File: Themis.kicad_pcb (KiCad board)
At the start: 2 copper layers, 100 x 50 mm, 47 parts, among them J1 SMA, J10 Conn_01x01, J11 Conn_01x01, J12 Conn_01x01, J13 Conn_01x01, J14 SMA, J15 SMA, J16 SMA, J17 SMA, J18 Conn_01x01, J2 SMA, J20 Conn_01x01, J3 SMA, J4 SMA, J5 Conn_01x05, J6 SMA, J7 SMA, J8 SMA, J9 SMA, T1 Tr 1/33, T2 Tr 33/1, U1 LMC6482

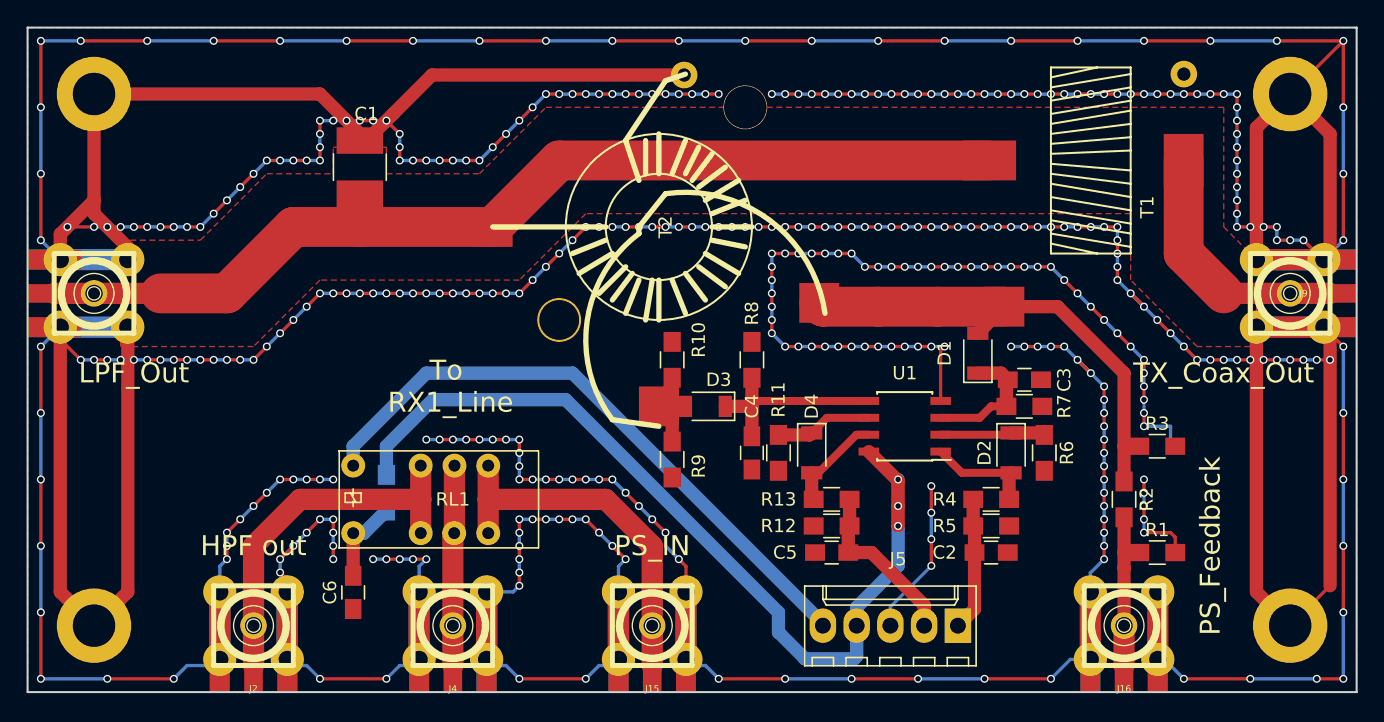
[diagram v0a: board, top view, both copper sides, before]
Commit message: BAT54 and transformer shielding added
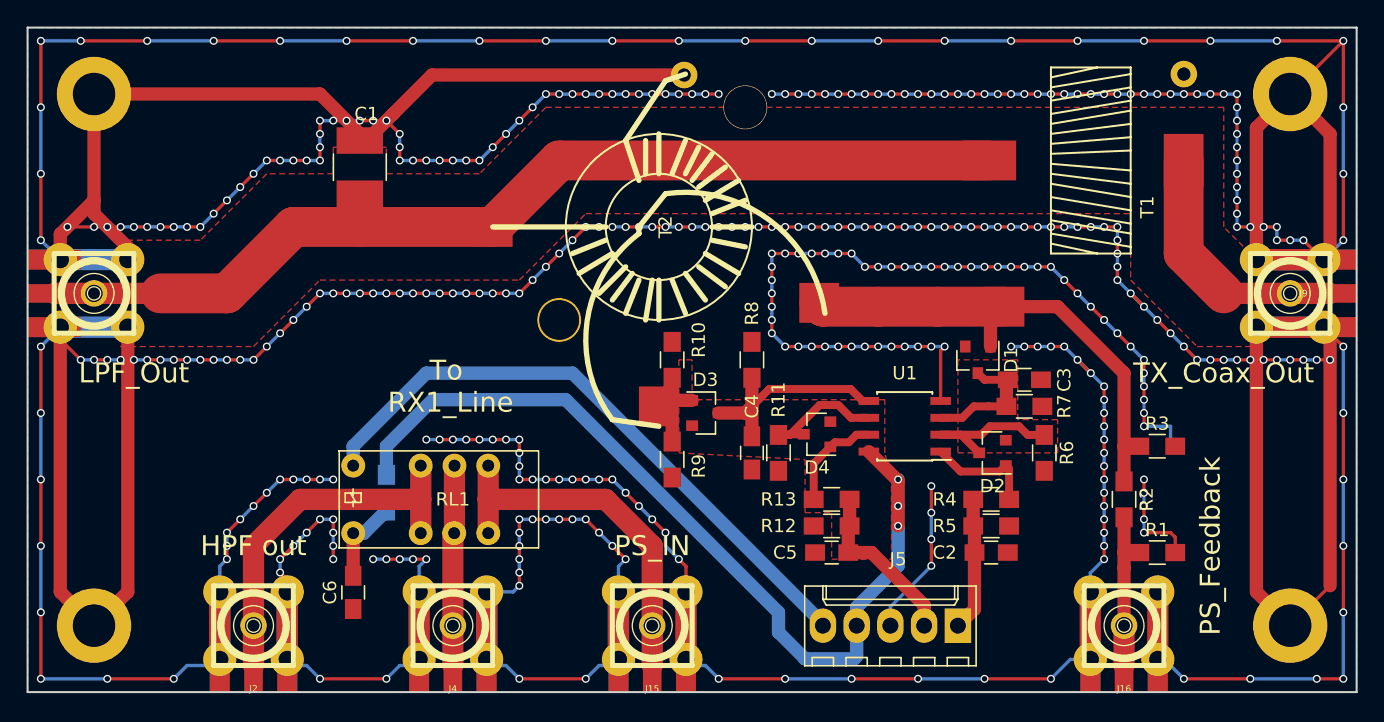
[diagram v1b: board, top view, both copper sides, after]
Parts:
- D1, D2, D3, D4: value D -> BAT54; footprint Diodes_SMD:D_1206 -> Diodes_SMD:D_SOT-23_ANK
- moved D4 1.46 mm to (149.4, 115.6), turned to 180 degrees
- moved D2 1.40 mm to (162.6, 117.0), turned to 180 degrees
- moved D1 0.50 mm to (161.5, 110.0), turned to 270 degrees
- moved D3 0.50 mm to (141.0, 114.0), turned to 0 degrees
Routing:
- net Net-(D2-Pad1): track 7.92 -> 11.8 mm
- net Net-(D4-Pad1): track 7.33 -> 10.1 mm
- net Net-(C4-Pad1): track 15.4 -> 16.8 mm
- net Net-(D3-Pad2): track 7.63 -> 8.31 mm
- net Net-(D1-Pad2): track 37.3 -> 37.9 mm

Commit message: via stitching added, new gerber
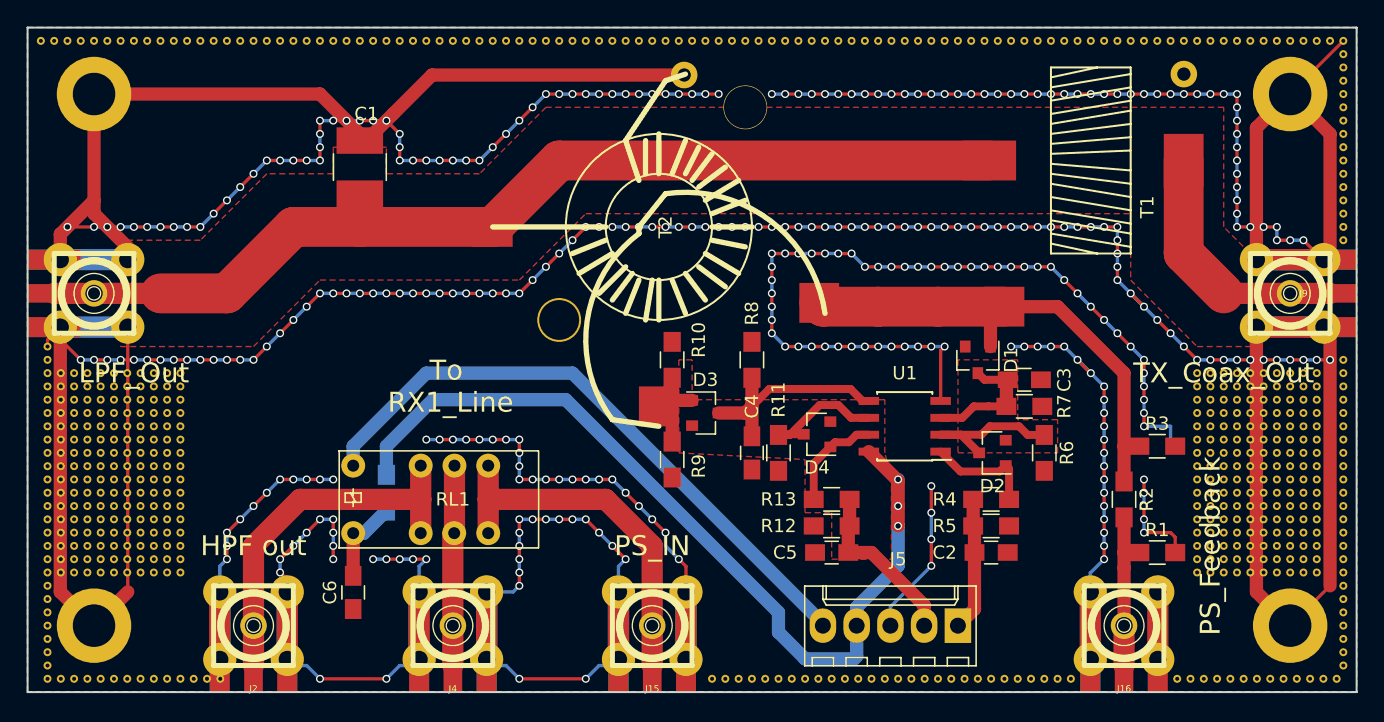
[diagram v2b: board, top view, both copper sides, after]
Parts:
- added REF**: via, via:via, F.Cu at (189.0, 101.0)
- added REF**: via, via:via, F.Cu at (189.0, 92.0)
- added REF**: via, via:via, F.Cu at (91.5, 128.0)
- added REF**: via, via:via, F.Cu at (91.5, 127.0)
- added REF**: via, via:via, F.Cu at (91.5, 126.0)
- added REF**: via, via:via, F.Cu at (91.5, 125.0)
- added REF**: via, via:via, F.Cu at (91.5, 124.0)
- added REF**: via, via:via, F.Cu at (91.5, 123.0)
- added REF**: via, via:via, F.Cu at (91.5, 122.0)
- added REF**: via, via:via, F.Cu at (91.5, 121.0)
- added REF**: via, via:via, F.Cu at (91.5, 120.0)
- added REF**: via, via:via, F.Cu at (91.5, 119.0)
- added REF**: via, via:via, F.Cu at (189.0, 91.0)
- added REF**: via, via:via, F.Cu at (91.5, 118.0)
- added REF**: via, via:via, F.Cu at (91.5, 117.0)
- added REF**: via, via:via, F.Cu at (91.5, 116.0)
- added REF**: via, via:via, F.Cu at (91.5, 115.0)
- added REF**: via, via:via, F.Cu at (91.5, 114.0)
- added REF**: via, via:via, F.Cu at (91.5, 113.0)
- added REF**: via, via:via, F.Cu at (91.5, 112.0)
- added REF**: via, via:via, F.Cu at (91.5, 111.0)
- added REF**: via, via:via, F.Cu at (91.5, 110.0)
- added REF**: via, via:via, F.Cu at (91.5, 109.0)
- added REF**: via, via:via, F.Cu at (189.0, 90.0)
- added REF**: via, via:via, F.Cu at (189.0, 86.0)
- added REF**: via, via:via, F.Cu at (188.0, 86.0)
- added REF**: via, via:via, F.Cu at (187.0, 86.0)
- added REF**: via, via:via, F.Cu at (186.0, 86.0)
- added REF**: via, via:via, F.Cu at (185.0, 86.0)
- added REF**: via, via:via, F.Cu at (184.0, 86.0)
- added REF**: via, via:via, F.Cu at (183.0, 86.0)
- added REF**: via, via:via, F.Cu at (182.0, 86.0)
- added REF**: via, via:via, F.Cu at (181.0, 86.0)
- added REF**: via, via:via, F.Cu at (180.0, 86.0)
- added REF**: via, via:via, F.Cu at (189.0, 89.0)
- added REF**: via, via:via, F.Cu at (179.0, 86.0)
- added REF**: via, via:via, F.Cu at (178.0, 86.0)
- added REF**: via, via:via, F.Cu at (177.0, 86.0)
- added REF**: via, via:via, F.Cu at (176.0, 86.0)
- added REF**: via, via:via, F.Cu at (175.0, 86.0)
- added REF**: via, via:via, F.Cu at (174.0, 86.0)
- added REF**: via, via:via, F.Cu at (173.0, 86.0)
- added REF**: via, via:via, F.Cu at (172.0, 86.0)
- added REF**: via, via:via, F.Cu at (171.0, 86.0)
- added REF**: via, via:via, F.Cu at (170.0, 86.0)
- added REF**: via, via:via, F.Cu at (189.0, 88.0)
- added REF**: via, via:via, F.Cu at (169.0, 86.0)
- added REF**: via, via:via, F.Cu at (168.0, 86.0)
- added REF**: via, via:via, F.Cu at (167.0, 86.0)
- added REF**: via, via:via, F.Cu at (166.0, 86.0)
- added REF**: via, via:via, F.Cu at (165.0, 86.0)
- added REF**: via, via:via, F.Cu at (164.0, 86.0)
- added REF**: via, via:via, F.Cu at (163.0, 86.0)
- added REF**: via, via:via, F.Cu at (162.0, 86.0)
- added REF**: via, via:via, F.Cu at (161.0, 86.0)
- added REF**: via, via:via, F.Cu at (160.0, 86.0)
- added REF**: via, via:via, F.Cu at (189.0, 87.0)
- added REF**: via, via:via, F.Cu at (159.0, 86.0)
- added REF**: via, via:via, F.Cu at (158.0, 86.0)
- added REF**: via, via:via, F.Cu at (157.0, 86.0)
- added REF**: via, via:via, F.Cu at (156.0, 86.0)
- added REF**: via, via:via, F.Cu at (155.0, 86.0)
- added REF**: via, via:via, F.Cu at (154.0, 86.0)
- added REF**: via, via:via, F.Cu at (153.0, 86.0)
- added REF**: via, via:via, F.Cu at (152.0, 86.0)
- added REF**: via, via:via, F.Cu at (151.0, 86.0)
- added REF**: via, via:via, F.Cu at (150.0, 86.0)
- added REF**: via, via:via, F.Cu at (189.0, 133.0)
- added REF**: via, via:via, F.Cu at (149.0, 86.0)
- added REF**: via, via:via, F.Cu at (148.0, 86.0)
- added REF**: via, via:via, F.Cu at (147.0, 86.0)
- added REF**: via, via:via, F.Cu at (146.0, 86.0)
- added REF**: via, via:via, F.Cu at (145.0, 86.0)
- added REF**: via, via:via, F.Cu at (144.0, 86.0)
- added REF**: via, via:via, F.Cu at (143.0, 86.0)
- added REF**: via, via:via, F.Cu at (142.0, 86.0)
- added REF**: via, via:via, F.Cu at (141.0, 86.0)
- added REF**: via, via:via, F.Cu at (140.0, 86.0)
- added REF**: via, via:via, F.Cu at (189.0, 132.0)
- added REF**: via, via:via, F.Cu at (139.0, 86.0)
- added REF**: via, via:via, F.Cu at (138.0, 86.0)
- added REF**: via, via:via, F.Cu at (137.0, 86.0)
- added REF**: via, via:via, F.Cu at (136.0, 86.0)
- added REF**: via, via:via, F.Cu at (135.0, 86.0)
- added REF**: via, via:via, F.Cu at (134.0, 86.0)
- added REF**: via, via:via, F.Cu at (133.0, 86.0)
- added REF**: via, via:via, F.Cu at (132.0, 86.0)
- added REF**: via, via:via, F.Cu at (131.0, 86.0)
- added REF**: via, via:via, F.Cu at (130.0, 86.0)
- added REF**: via, via:via, F.Cu at (189.0, 131.0)
- added REF**: via, via:via, F.Cu at (129.0, 86.0)
- added REF**: via, via:via, F.Cu at (128.0, 86.0)
- added REF**: via, via:via, F.Cu at (127.0, 86.0)
- added REF**: via, via:via, F.Cu at (126.0, 86.0)
- added REF**: via, via:via, F.Cu at (125.0, 86.0)
- added REF**: via, via:via, F.Cu at (124.0, 86.0)
- added REF**: via, via:via, F.Cu at (123.0, 86.0)
- added REF**: via, via:via, F.Cu at (122.0, 86.0)
- added REF**: via, via:via, F.Cu at (121.0, 86.0)
- added REF**: via, via:via, F.Cu at (120.0, 86.0)
- added REF**: via, via:via, F.Cu at (189.0, 130.0)
- added REF**: via, via:via, F.Cu at (119.0, 86.0)
- added REF**: via, via:via, F.Cu at (118.0, 86.0)
- added REF**: via, via:via, F.Cu at (117.0, 86.0)
- added REF**: via, via:via, F.Cu at (116.0, 86.0)
- added REF**: via, via:via, F.Cu at (115.0, 86.0)
- added REF**: via, via:via, F.Cu at (114.0, 86.0)
- added REF**: via, via:via, F.Cu at (113.0, 86.0)
- added REF**: via, via:via, F.Cu at (112.0, 86.0)
- added REF**: via, via:via, F.Cu at (111.0, 86.0)
- added REF**: via, via:via, F.Cu at (110.0, 86.0)
- added REF**: via, via:via, F.Cu at (189.0, 100.0)
- added REF**: via, via:via, F.Cu at (189.0, 129.0)
- added REF**: via, via:via, F.Cu at (109.0, 86.0)
- added REF**: via, via:via, F.Cu at (108.0, 86.0)
- added REF**: via, via:via, F.Cu at (107.0, 86.0)
- added REF**: via, via:via, F.Cu at (106.0, 86.0)
- added REF**: via, via:via, F.Cu at (105.0, 86.0)
- added REF**: via, via:via, F.Cu at (104.0, 86.0)
- added REF**: via, via:via, F.Cu at (103.0, 86.0)
- added REF**: via, via:via, F.Cu at (102.0, 86.0)
- added REF**: via, via:via, F.Cu at (101.0, 86.0)
- added REF**: via, via:via, F.Cu at (100.0, 86.0)
- added REF**: via, via:via, F.Cu at (189.0, 128.0)
- added REF**: via, via:via, F.Cu at (99.0, 86.0)
- added REF**: via, via:via, F.Cu at (98.0, 86.0)
- added REF**: via, via:via, F.Cu at (97.0, 86.0)
- added REF**: via, via:via, F.Cu at (96.0, 86.0)
- added REF**: via, via:via, F.Cu at (95.0, 86.0)
- added REF**: via, via:via, F.Cu at (94.0, 86.0)
- added REF**: via, via:via, F.Cu at (93.0, 86.0)
- added REF**: via, via:via, F.Cu at (92.0, 86.0)
- added REF**: via, via:via, F.Cu at (101.5, 126.0)
- added REF**: via, via:via, F.Cu at (100.5, 126.0)
- added REF**: via, via:via, F.Cu at (189.0, 127.0)
- added REF**: via, via:via, F.Cu at (99.5, 126.0)
- added REF**: via, via:via, F.Cu at (98.5, 126.0)
- added REF**: via, via:via, F.Cu at (97.5, 126.0)
- added REF**: via, via:via, F.Cu at (96.5, 126.0)
- added REF**: via, via:via, F.Cu at (95.5, 126.0)
- added REF**: via, via:via, F.Cu at (94.5, 126.0)
- added REF**: via, via:via, F.Cu at (93.5, 126.0)
- added REF**: via, via:via, F.Cu at (92.5, 126.0)
- added REF**: via, via:via, F.Cu at (101.5, 125.0)
- added REF**: via, via:via, F.Cu at (100.5, 125.0)
- added REF**: via, via:via, F.Cu at (189.0, 126.0)
- added REF**: via, via:via, F.Cu at (99.5, 125.0)
- added REF**: via, via:via, F.Cu at (98.5, 125.0)
- added REF**: via, via:via, F.Cu at (97.5, 125.0)
- added REF**: via, via:via, F.Cu at (96.5, 125.0)
- added REF**: via, via:via, F.Cu at (95.5, 125.0)
- added REF**: via, via:via, F.Cu at (94.5, 125.0)
- added REF**: via, via:via, F.Cu at (93.5, 125.0)
- added REF**: via, via:via, F.Cu at (92.5, 125.0)
- added REF**: via, via:via, F.Cu at (101.5, 124.0)
- added REF**: via, via:via, F.Cu at (100.5, 124.0)
- added REF**: via, via:via, F.Cu at (189.0, 125.0)
- added REF**: via, via:via, F.Cu at (99.5, 124.0)
- added REF**: via, via:via, F.Cu at (98.5, 124.0)
- added REF**: via, via:via, F.Cu at (97.5, 124.0)
- added REF**: via, via:via, F.Cu at (96.5, 124.0)
- added REF**: via, via:via, F.Cu at (95.5, 124.0)
- added REF**: via, via:via, F.Cu at (94.5, 124.0)
- added REF**: via, via:via, F.Cu at (93.5, 124.0)
- added REF**: via, via:via, F.Cu at (92.5, 124.0)
- added REF**: via, via:via, F.Cu at (101.5, 123.0)
- added REF**: via, via:via, F.Cu at (100.5, 123.0)
- added REF**: via, via:via, F.Cu at (189.0, 124.0)
- added REF**: via, via:via, F.Cu at (99.5, 123.0)
- added REF**: via, via:via, F.Cu at (98.5, 123.0)
- added REF**: via, via:via, F.Cu at (97.5, 123.0)
- added REF**: via, via:via, F.Cu at (96.5, 123.0)
- added REF**: via, via:via, F.Cu at (95.5, 123.0)
- added REF**: via, via:via, F.Cu at (94.5, 123.0)
- added REF**: via, via:via, F.Cu at (93.5, 123.0)
- added REF**: via, via:via, F.Cu at (92.5, 123.0)
- added REF**: via, via:via, F.Cu at (101.5, 122.0)
- added REF**: via, via:via, F.Cu at (100.5, 122.0)
- added REF**: via, via:via, F.Cu at (189.0, 123.0)
- added REF**: via, via:via, F.Cu at (99.5, 122.0)
- added REF**: via, via:via, F.Cu at (98.5, 122.0)
- added REF**: via, via:via, F.Cu at (97.5, 122.0)
- added REF**: via, via:via, F.Cu at (96.5, 122.0)
- added REF**: via, via:via, F.Cu at (95.5, 122.0)
- added REF**: via, via:via, F.Cu at (94.5, 122.0)
- added REF**: via, via:via, F.Cu at (93.5, 122.0)
- added REF**: via, via:via, F.Cu at (92.5, 122.0)
- added REF**: via, via:via, F.Cu at (101.5, 121.0)
- added REF**: via, via:via, F.Cu at (100.5, 121.0)
- added REF**: via, via:via, F.Cu at (189.0, 122.0)
- added REF**: via, via:via, F.Cu at (99.5, 121.0)
- added REF**: via, via:via, F.Cu at (98.5, 121.0)
- added REF**: via, via:via, F.Cu at (97.5, 121.0)
- added REF**: via, via:via, F.Cu at (96.5, 121.0)
- added REF**: via, via:via, F.Cu at (95.5, 121.0)
- added REF**: via, via:via, F.Cu at (94.5, 121.0)
- added REF**: via, via:via, F.Cu at (93.5, 121.0)
- added REF**: via, via:via, F.Cu at (92.5, 121.0)
- added REF**: via, via:via, F.Cu at (101.5, 120.0)
- added REF**: via, via:via, F.Cu at (100.5, 120.0)
- added REF**: via, via:via, F.Cu at (189.0, 121.0)
- added REF**: via, via:via, F.Cu at (99.5, 120.0)
- added REF**: via, via:via, F.Cu at (98.5, 120.0)
- added REF**: via, via:via, F.Cu at (97.5, 120.0)
- added REF**: via, via:via, F.Cu at (96.5, 120.0)
- added REF**: via, via:via, F.Cu at (95.5, 120.0)
- added REF**: via, via:via, F.Cu at (94.5, 120.0)
- added REF**: via, via:via, F.Cu at (93.5, 120.0)
- added REF**: via, via:via, F.Cu at (92.5, 120.0)
- added REF**: via, via:via, F.Cu at (101.5, 119.0)
- added REF**: via, via:via, F.Cu at (100.5, 119.0)
- added REF**: via, via:via, F.Cu at (189.0, 120.0)
- added REF**: via, via:via, F.Cu at (99.5, 119.0)
- added REF**: via, via:via, F.Cu at (98.5, 119.0)
- added REF**: via, via:via, F.Cu at (97.5, 119.0)
- added REF**: via, via:via, F.Cu at (96.5, 119.0)
- added REF**: via, via:via, F.Cu at (95.5, 119.0)
- added REF**: via, via:via, F.Cu at (94.5, 119.0)
- added REF**: via, via:via, F.Cu at (93.5, 119.0)
- added REF**: via, via:via, F.Cu at (92.5, 119.0)
- added REF**: via, via:via, F.Cu at (101.5, 118.0)
- added REF**: via, via:via, F.Cu at (100.5, 118.0)
- added REF**: via, via:via, F.Cu at (189.0, 99.0)
- added REF**: via, via:via, F.Cu at (189.0, 119.0)
- added REF**: via, via:via, F.Cu at (99.5, 118.0)
- added REF**: via, via:via, F.Cu at (98.5, 118.0)
- added REF**: via, via:via, F.Cu at (97.5, 118.0)
- added REF**: via, via:via, F.Cu at (96.5, 118.0)
- added REF**: via, via:via, F.Cu at (95.5, 118.0)
- added REF**: via, via:via, F.Cu at (94.5, 118.0)
- added REF**: via, via:via, F.Cu at (93.5, 118.0)
- added REF**: via, via:via, F.Cu at (92.5, 118.0)
- added REF**: via, via:via, F.Cu at (101.5, 117.0)
- added REF**: via, via:via, F.Cu at (100.5, 117.0)
- added REF**: via, via:via, F.Cu at (189.0, 118.0)
- added REF**: via, via:via, F.Cu at (99.5, 117.0)
- added REF**: via, via:via, F.Cu at (98.5, 117.0)
- added REF**: via, via:via, F.Cu at (97.5, 117.0)
- added REF**: via, via:via, F.Cu at (96.5, 117.0)
- added REF**: via, via:via, F.Cu at (95.5, 117.0)
- added REF**: via, via:via, F.Cu at (94.5, 117.0)
- added REF**: via, via:via, F.Cu at (93.5, 117.0)
- added REF**: via, via:via, F.Cu at (92.5, 117.0)
- added REF**: via, via:via, F.Cu at (101.5, 116.0)
- added REF**: via, via:via, F.Cu at (100.5, 116.0)
- added REF**: via, via:via, F.Cu at (189.0, 117.0)
- added REF**: via, via:via, F.Cu at (99.5, 116.0)
- added REF**: via, via:via, F.Cu at (98.5, 116.0)
- added REF**: via, via:via, F.Cu at (97.5, 116.0)
- added REF**: via, via:via, F.Cu at (96.5, 116.0)
- added REF**: via, via:via, F.Cu at (95.5, 116.0)
- added REF**: via, via:via, F.Cu at (94.5, 116.0)
- added REF**: via, via:via, F.Cu at (93.5, 116.0)
- added REF**: via, via:via, F.Cu at (92.5, 116.0)
- added REF**: via, via:via, F.Cu at (101.5, 115.0)
- added REF**: via, via:via, F.Cu at (100.5, 115.0)
- added REF**: via, via:via, F.Cu at (189.0, 116.0)
- added REF**: via, via:via, F.Cu at (99.5, 115.0)
- added REF**: via, via:via, F.Cu at (98.5, 115.0)
- added REF**: via, via:via, F.Cu at (97.5, 115.0)
- added REF**: via, via:via, F.Cu at (96.5, 115.0)
- added REF**: via, via:via, F.Cu at (95.5, 115.0)
- added REF**: via, via:via, F.Cu at (94.5, 115.0)
- added REF**: via, via:via, F.Cu at (93.5, 115.0)
- added REF**: via, via:via, F.Cu at (92.5, 115.0)
- added REF**: via, via:via, F.Cu at (101.5, 114.0)
- added REF**: via, via:via, F.Cu at (100.5, 114.0)
- added REF**: via, via:via, F.Cu at (189.0, 115.0)
- added REF**: via, via:via, F.Cu at (99.5, 114.0)
- added REF**: via, via:via, F.Cu at (98.5, 114.0)
- added REF**: via, via:via, F.Cu at (97.5, 114.0)
- added REF**: via, via:via, F.Cu at (96.5, 114.0)
- added REF**: via, via:via, F.Cu at (95.5, 114.0)
- added REF**: via, via:via, F.Cu at (94.5, 114.0)
- added REF**: via, via:via, F.Cu at (93.5, 114.0)
- added REF**: via, via:via, F.Cu at (92.5, 114.0)
- added REF**: via, via:via, F.Cu at (101.5, 113.0)
- added REF**: via, via:via, F.Cu at (100.5, 113.0)
- added REF**: via, via:via, F.Cu at (189.0, 114.0)
- added REF**: via, via:via, F.Cu at (99.5, 113.0)
- added REF**: via, via:via, F.Cu at (98.5, 113.0)
- added REF**: via, via:via, F.Cu at (97.5, 113.0)
- added REF**: via, via:via, F.Cu at (96.5, 113.0)
- added REF**: via, via:via, F.Cu at (95.5, 113.0)
- added REF**: via, via:via, F.Cu at (94.5, 113.0)
- added REF**: via, via:via, F.Cu at (93.5, 113.0)
- added REF**: via, via:via, F.Cu at (92.5, 113.0)
- added REF**: via, via:via, F.Cu at (101.5, 112.0)
- added REF**: via, via:via, F.Cu at (100.5, 112.0)
- added REF**: via, via:via, F.Cu at (189.0, 113.0)
- added REF**: via, via:via, F.Cu at (99.5, 112.0)
- added REF**: via, via:via, F.Cu at (98.5, 112.0)
- added REF**: via, via:via, F.Cu at (97.5, 112.0)
- added REF**: via, via:via, F.Cu at (96.5, 112.0)
- added REF**: via, via:via, F.Cu at (95.5, 112.0)
- added REF**: via, via:via, F.Cu at (94.5, 112.0)
- added REF**: via, via:via, F.Cu at (93.5, 112.0)
- added REF**: via, via:via, F.Cu at (92.5, 112.0)
- added REF**: via, via:via, F.Cu at (101.5, 111.0)
- added REF**: via, via:via, F.Cu at (100.5, 111.0)
- added REF**: via, via:via, F.Cu at (189.0, 112.0)
- added REF**: via, via:via, F.Cu at (99.5, 111.0)
- added REF**: via, via:via, F.Cu at (98.5, 111.0)
- added REF**: via, via:via, F.Cu at (97.5, 111.0)
- added REF**: via, via:via, F.Cu at (96.5, 111.0)
- added REF**: via, via:via, F.Cu at (95.5, 111.0)
- added REF**: via, via:via, F.Cu at (94.5, 111.0)
- added REF**: via, via:via, F.Cu at (93.5, 111.0)
- added REF**: via, via:via, F.Cu at (187.0, 126.0)
- added REF**: via, via:via, F.Cu at (186.0, 126.0)
- added REF**: via, via:via, F.Cu at (185.0, 126.0)
- added REF**: via, via:via, F.Cu at (189.0, 111.0)
- added REF**: via, via:via, F.Cu at (184.0, 126.0)
- added REF**: via, via:via, F.Cu at (183.0, 126.0)
- added REF**: via, via:via, F.Cu at (182.0, 126.0)
- added REF**: via, via:via, F.Cu at (181.0, 126.0)
- added REF**: via, via:via, F.Cu at (180.0, 126.0)
- added REF**: via, via:via, F.Cu at (179.0, 126.0)
- added REF**: via, via:via, F.Cu at (178.0, 126.0)
- added REF**: via, via:via, F.Cu at (187.0, 125.0)
- added REF**: via, via:via, F.Cu at (186.0, 125.0)
- added REF**: via, via:via, F.Cu at (185.0, 125.0)
- added REF**: via, via:via, F.Cu at (189.0, 110.0)
- added REF**: via, via:via, F.Cu at (184.0, 125.0)
- added REF**: via, via:via, F.Cu at (183.0, 125.0)
- added REF**: via, via:via, F.Cu at (182.0, 125.0)
- added REF**: via, via:via, F.Cu at (181.0, 125.0)
- added REF**: via, via:via, F.Cu at (180.0, 125.0)
- added REF**: via, via:via, F.Cu at (179.0, 125.0)
- added REF**: via, via:via, F.Cu at (178.0, 125.0)
- added REF**: via, via:via, F.Cu at (187.0, 124.0)
- added REF**: via, via:via, F.Cu at (186.0, 124.0)
- added REF**: via, via:via, F.Cu at (185.0, 124.0)
- added REF**: via, via:via, F.Cu at (189.0, 98.0)
- added REF**: via, via:via, F.Cu at (188.5, 134.0)
- added REF**: via, via:via, F.Cu at (184.0, 124.0)
- added REF**: via, via:via, F.Cu at (183.0, 124.0)
- added REF**: via, via:via, F.Cu at (182.0, 124.0)
- added REF**: via, via:via, F.Cu at (181.0, 124.0)
- added REF**: via, via:via, F.Cu at (180.0, 124.0)
- added REF**: via, via:via, F.Cu at (179.0, 124.0)
- added REF**: via, via:via, F.Cu at (178.0, 124.0)
- added REF**: via, via:via, F.Cu at (187.0, 123.0)
- added REF**: via, via:via, F.Cu at (186.0, 123.0)
- added REF**: via, via:via, F.Cu at (185.0, 123.0)
- added REF**: via, via:via, F.Cu at (187.5, 134.0)
- added REF**: via, via:via, F.Cu at (184.0, 123.0)
- added REF**: via, via:via, F.Cu at (183.0, 123.0)
- added REF**: via, via:via, F.Cu at (182.0, 123.0)
- added REF**: via, via:via, F.Cu at (181.0, 123.0)
- added REF**: via, via:via, F.Cu at (180.0, 123.0)
- added REF**: via, via:via, F.Cu at (179.0, 123.0)
- added REF**: via, via:via, F.Cu at (178.0, 123.0)
- added REF**: via, via:via, F.Cu at (187.0, 122.0)
- added REF**: via, via:via, F.Cu at (186.0, 122.0)
- added REF**: via, via:via, F.Cu at (185.0, 122.0)
- added REF**: via, via:via, F.Cu at (186.5, 134.0)
- added REF**: via, via:via, F.Cu at (184.0, 122.0)
- added REF**: via, via:via, F.Cu at (183.0, 122.0)
- added REF**: via, via:via, F.Cu at (182.0, 122.0)
- added REF**: via, via:via, F.Cu at (181.0, 122.0)
- added REF**: via, via:via, F.Cu at (180.0, 122.0)
- added REF**: via, via:via, F.Cu at (179.0, 122.0)
- added REF**: via, via:via, F.Cu at (178.0, 122.0)
- added REF**: via, via:via, F.Cu at (187.0, 121.0)
- added REF**: via, via:via, F.Cu at (186.0, 121.0)
- added REF**: via, via:via, F.Cu at (185.0, 121.0)
- added REF**: via, via:via, F.Cu at (185.5, 134.0)
- added REF**: via, via:via, F.Cu at (184.0, 121.0)
- added REF**: via, via:via, F.Cu at (183.0, 121.0)
- added REF**: via, via:via, F.Cu at (182.0, 121.0)
- added REF**: via, via:via, F.Cu at (181.0, 121.0)
- added REF**: via, via:via, F.Cu at (180.0, 121.0)
- added REF**: via, via:via, F.Cu at (179.0, 121.0)
- added REF**: via, via:via, F.Cu at (178.0, 121.0)
- added REF**: via, via:via, F.Cu at (187.0, 120.0)
- added REF**: via, via:via, F.Cu at (186.0, 120.0)
- added REF**: via, via:via, F.Cu at (185.0, 120.0)
- added REF**: via, via:via, F.Cu at (184.5, 134.0)
- added REF**: via, via:via, F.Cu at (184.0, 120.0)
- added REF**: via, via:via, F.Cu at (183.0, 120.0)
- added REF**: via, via:via, F.Cu at (182.0, 120.0)
- added REF**: via, via:via, F.Cu at (181.0, 120.0)
- added REF**: via, via:via, F.Cu at (180.0, 120.0)
- added REF**: via, via:via, F.Cu at (179.0, 120.0)
- added REF**: via, via:via, F.Cu at (178.0, 120.0)
- added REF**: via, via:via, F.Cu at (187.0, 119.0)
- added REF**: via, via:via, F.Cu at (186.0, 119.0)
- added REF**: via, via:via, F.Cu at (185.0, 119.0)
- added REF**: via, via:via, F.Cu at (183.5, 134.0)
- added REF**: via, via:via, F.Cu at (184.0, 119.0)
- added REF**: via, via:via, F.Cu at (183.0, 119.0)
- added REF**: via, via:via, F.Cu at (182.0, 119.0)
- added REF**: via, via:via, F.Cu at (181.0, 119.0)
- added REF**: via, via:via, F.Cu at (180.0, 119.0)
- added REF**: via, via:via, F.Cu at (179.0, 119.0)
- added REF**: via, via:via, F.Cu at (178.0, 119.0)
- added REF**: via, via:via, F.Cu at (187.0, 118.0)
- added REF**: via, via:via, F.Cu at (186.0, 118.0)
- added REF**: via, via:via, F.Cu at (185.0, 118.0)
- added REF**: via, via:via, F.Cu at (182.5, 134.0)
- added REF**: via, via:via, F.Cu at (184.0, 118.0)
- added REF**: via, via:via, F.Cu at (183.0, 118.0)
- added REF**: via, via:via, F.Cu at (182.0, 118.0)
- added REF**: via, via:via, F.Cu at (181.0, 118.0)
- added REF**: via, via:via, F.Cu at (180.0, 118.0)
- added REF**: via, via:via, F.Cu at (179.0, 118.0)
- added REF**: via, via:via, F.Cu at (178.0, 118.0)
- added REF**: via, via:via, F.Cu at (187.0, 117.0)
- added REF**: via, via:via, F.Cu at (186.0, 117.0)
- added REF**: via, via:via, F.Cu at (185.0, 117.0)
- added REF**: via, via:via, F.Cu at (181.5, 134.0)
- added REF**: via, via:via, F.Cu at (184.0, 117.0)
- added REF**: via, via:via, F.Cu at (183.0, 117.0)
- added REF**: via, via:via, F.Cu at (182.0, 117.0)
- added REF**: via, via:via, F.Cu at (181.0, 117.0)
- added REF**: via, via:via, F.Cu at (180.0, 117.0)
- added REF**: via, via:via, F.Cu at (179.0, 117.0)
- added REF**: via, via:via, F.Cu at (178.0, 117.0)
- added REF**: via, via:via, F.Cu at (187.0, 116.0)
- added REF**: via, via:via, F.Cu at (186.0, 116.0)
- added REF**: via, via:via, F.Cu at (185.0, 116.0)
- added REF**: via, via:via, F.Cu at (180.5, 134.0)
- added REF**: via, via:via, F.Cu at (184.0, 116.0)
- added REF**: via, via:via, F.Cu at (183.0, 116.0)
- added REF**: via, via:via, F.Cu at (182.0, 116.0)
- added REF**: via, via:via, F.Cu at (181.0, 116.0)
- added REF**: via, via:via, F.Cu at (180.0, 116.0)
- added REF**: via, via:via, F.Cu at (179.0, 116.0)
- added REF**: via, via:via, F.Cu at (178.0, 116.0)
- added REF**: via, via:via, F.Cu at (187.0, 115.0)
- added REF**: via, via:via, F.Cu at (186.0, 115.0)
- added REF**: via, via:via, F.Cu at (185.0, 115.0)
- added REF**: via, via:via, F.Cu at (179.5, 134.0)
- added REF**: via, via:via, F.Cu at (184.0, 115.0)
- added REF**: via, via:via, F.Cu at (183.0, 115.0)
- added REF**: via, via:via, F.Cu at (182.0, 115.0)
- added REF**: via, via:via, F.Cu at (181.0, 115.0)
- added REF**: via, via:via, F.Cu at (180.0, 115.0)
- added REF**: via, via:via, F.Cu at (179.0, 115.0)
- added REF**: via, via:via, F.Cu at (178.0, 115.0)
- added REF**: via, via:via, F.Cu at (187.0, 114.0)
- added REF**: via, via:via, F.Cu at (186.0, 114.0)
- added REF**: via, via:via, F.Cu at (185.0, 114.0)
- added REF**: via, via:via, F.Cu at (189.0, 97.0)
- added REF**: via, via:via, F.Cu at (178.5, 134.0)
- added REF**: via, via:via, F.Cu at (184.0, 114.0)
- added REF**: via, via:via, F.Cu at (183.0, 114.0)
- added REF**: via, via:via, F.Cu at (182.0, 114.0)
- added REF**: via, via:via, F.Cu at (181.0, 114.0)
- added REF**: via, via:via, F.Cu at (180.0, 114.0)
- added REF**: via, via:via, F.Cu at (179.0, 114.0)
- added REF**: via, via:via, F.Cu at (178.0, 114.0)
- added REF**: via, via:via, F.Cu at (187.0, 113.0)
- added REF**: via, via:via, F.Cu at (186.0, 113.0)
- added REF**: via, via:via, F.Cu at (185.0, 113.0)
- added REF**: via, via:via, F.Cu at (177.5, 134.0)
- added REF**: via, via:via, F.Cu at (184.0, 113.0)
- added REF**: via, via:via, F.Cu at (183.0, 113.0)
- added REF**: via, via:via, F.Cu at (182.0, 113.0)
- added REF**: via, via:via, F.Cu at (181.0, 113.0)
- added REF**: via, via:via, F.Cu at (180.0, 113.0)
- added REF**: via, via:via, F.Cu at (179.0, 113.0)
- added REF**: via, via:via, F.Cu at (178.0, 113.0)
- added REF**: via, via:via, F.Cu at (187.0, 112.0)
- added REF**: via, via:via, F.Cu at (186.0, 112.0)
- added REF**: via, via:via, F.Cu at (185.0, 112.0)
- added REF**: via, via:via, F.Cu at (176.5, 134.0)
- added REF**: via, via:via, F.Cu at (184.0, 112.0)
- added REF**: via, via:via, F.Cu at (183.0, 112.0)
- added REF**: via, via:via, F.Cu at (182.0, 112.0)
- added REF**: via, via:via, F.Cu at (181.0, 112.0)
- added REF**: via, via:via, F.Cu at (180.0, 112.0)
- added REF**: via, via:via, F.Cu at (179.0, 112.0)
- added REF**: via, via:via, F.Cu at (178.0, 112.0)
- added REF**: via, via:via, F.Cu at (187.0, 111.0)
- added REF**: via, via:via, F.Cu at (186.0, 111.0)
- added REF**: via, via:via, F.Cu at (185.0, 111.0)
- added REF**: via, via:via, F.Cu at (168.5, 134.0)
- added REF**: via, via:via, F.Cu at (184.0, 111.0)
- added REF**: via, via:via, F.Cu at (183.0, 111.0)
- added REF**: via, via:via, F.Cu at (182.0, 111.0)
- added REF**: via, via:via, F.Cu at (181.0, 111.0)
- added REF**: via, via:via, F.Cu at (180.0, 111.0)
- added REF**: via, via:via, F.Cu at (179.0, 111.0)
- added REF**: via, via:via, F.Cu at (92.5, 111.0)
- added REF**: via, via:via, F.Cu at (178.0, 111.0)
- added REF**: via, via:via, F.Cu at (91.0, 86.0)
- added REF**: via, via:via, F.Cu at (167.5, 134.0)
- added REF**: via, via:via, F.Cu at (166.5, 134.0)
- added REF**: via, via:via, F.Cu at (165.5, 134.0)
- added REF**: via, via:via, F.Cu at (164.5, 134.0)
- added REF**: via, via:via, F.Cu at (163.5, 134.0)
- added REF**: via, via:via, F.Cu at (162.5, 134.0)
- added REF**: via, via:via, F.Cu at (189.0, 96.0)
- added REF**: via, via:via, F.Cu at (161.5, 134.0)
- added REF**: via, via:via, F.Cu at (160.5, 134.0)
- added REF**: via, via:via, F.Cu at (159.5, 134.0)
- added REF**: via, via:via, F.Cu at (158.5, 134.0)
- added REF**: via, via:via, F.Cu at (157.5, 134.0)
- added REF**: via, via:via, F.Cu at (156.5, 134.0)
- added REF**: via, via:via, F.Cu at (155.5, 134.0)
- added REF**: via, via:via, F.Cu at (154.5, 134.0)
- added REF**: via, via:via, F.Cu at (153.5, 134.0)
- added REF**: via, via:via, F.Cu at (152.5, 134.0)
- added REF**: via, via:via, F.Cu at (189.0, 95.0)
- added REF**: via, via:via, F.Cu at (151.5, 134.0)
- added REF**: via, via:via, F.Cu at (150.5, 134.0)
- added REF**: via, via:via, F.Cu at (149.5, 134.0)
- added REF**: via, via:via, F.Cu at (148.5, 134.0)
- added REF**: via, via:via, F.Cu at (147.5, 134.0)
- added REF**: via, via:via, F.Cu at (146.5, 134.0)
- added REF**: via, via:via, F.Cu at (145.5, 134.0)
- added REF**: via, via:via, F.Cu at (144.5, 134.0)
- added REF**: via, via:via, F.Cu at (143.5, 134.0)
- added REF**: via, via:via, F.Cu at (142.5, 134.0)
- added REF**: via, via:via, F.Cu at (189.0, 94.0)
- added REF**: via, via:via, F.Cu at (141.5, 134.0)
- added REF**: via, via:via, F.Cu at (104.5, 134.0)
- added REF**: via, via:via, F.Cu at (103.5, 134.0)
- added REF**: via, via:via, F.Cu at (102.5, 134.0)
- added REF**: via, via:via, F.Cu at (101.5, 134.0)
- added REF**: via, via:via, F.Cu at (100.5, 134.0)
- added REF**: via, via:via, F.Cu at (99.5, 134.0)
- added REF**: via, via:via, F.Cu at (98.5, 134.0)
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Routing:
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
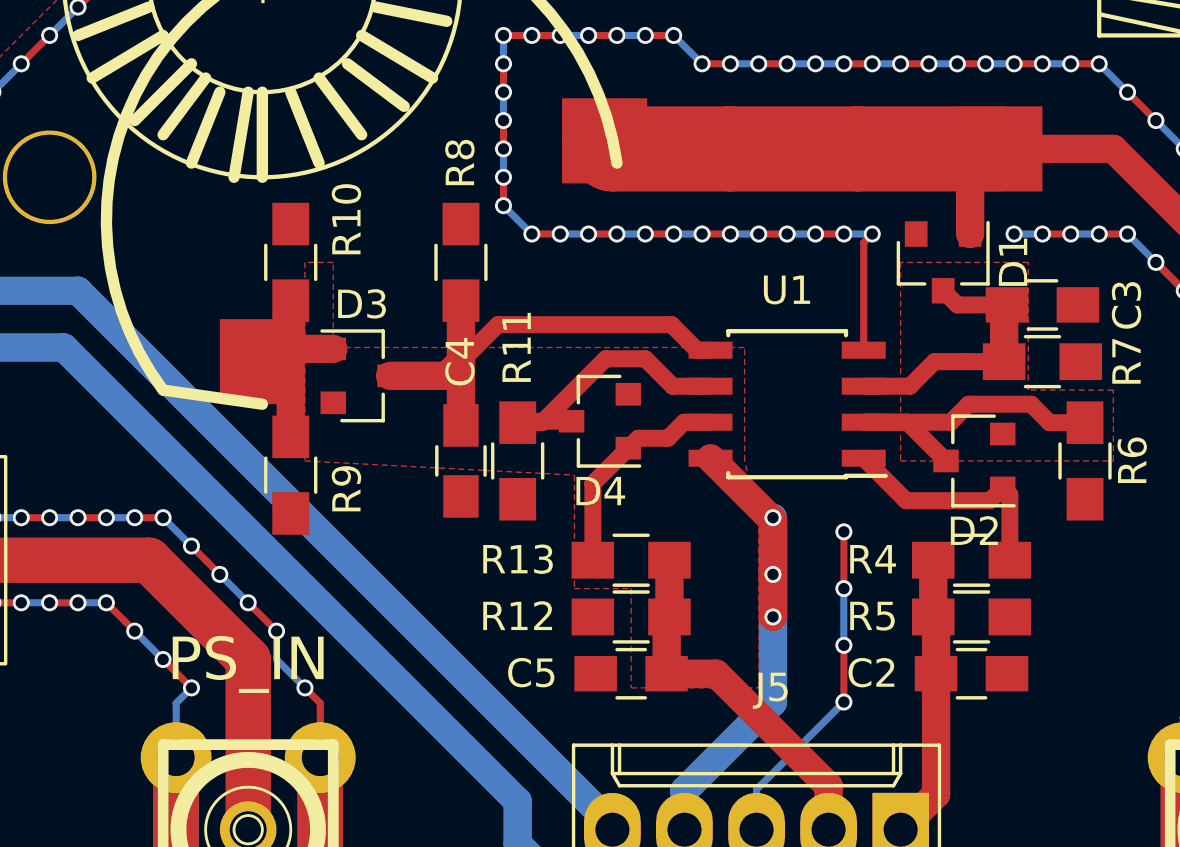
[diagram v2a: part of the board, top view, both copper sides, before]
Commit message: silkmask cleaning, new gerber
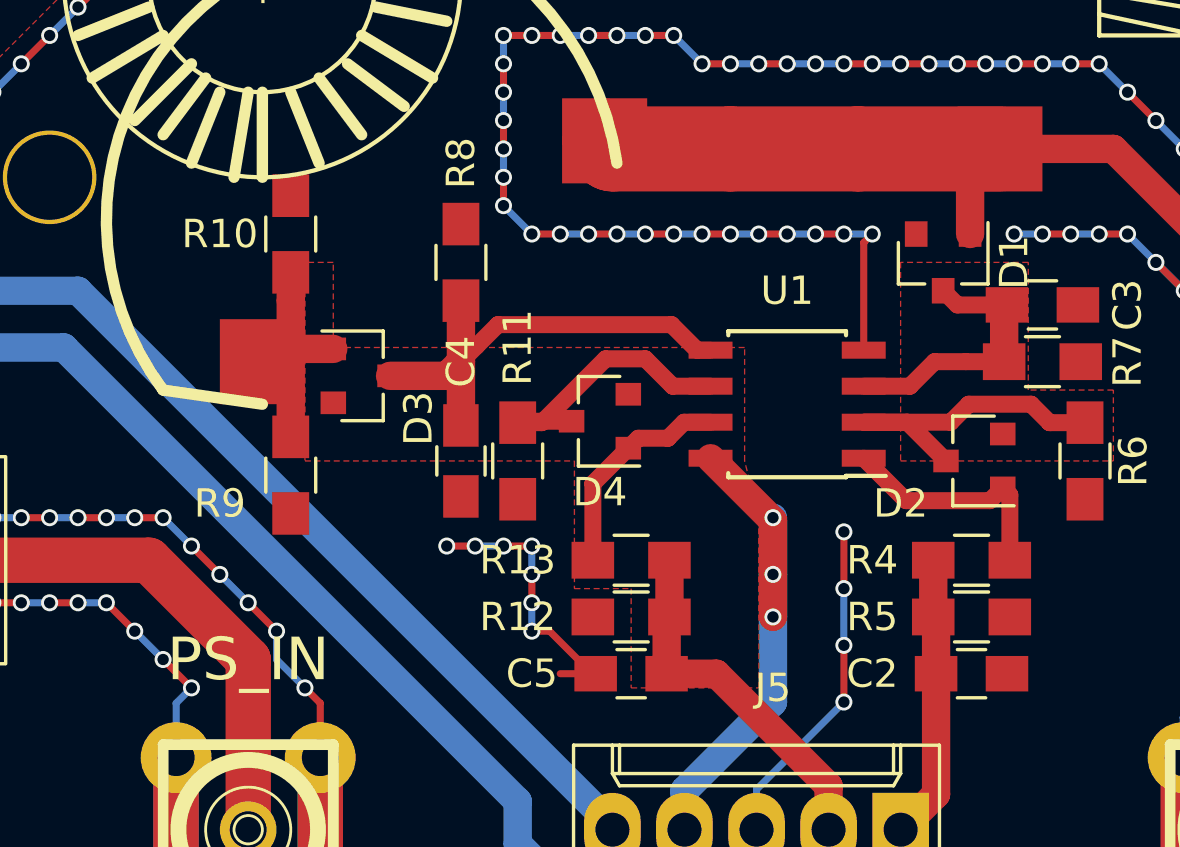
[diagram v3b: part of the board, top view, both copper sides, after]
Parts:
- moved R10 1.00 mm to (138.5, 109.0)
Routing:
- net GND: track 751.4 -> 761.5 mm, vias 354 -> 361
- net Net-(D3-Pad2): track 8.31 -> 9.31 mm
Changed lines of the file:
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@@
     (links 661)
     (no_connects 0)
-    (area 80.724999 82.899999 225.428571 177.05)
+    (area 89.924999 84.924999 190.075001 135.075001)
     (thickness 1.6)
     (drawings 14)
-    (tracks 933)
+    (tracks 951)
     (zones 0)
     (modules 585)
@@
     (tags "resistor 0805")
     (attr smd)
-    (fp_text reference R9 (at 0.5 -2 270) (layer F.SilkS)
+    (fp_text reference R9 (at 1 2.5 360) (layer F.SilkS)
       (effects (font (size 1 1) (thickness 0.15)))
     )
@@
   )
   (module Resistors_SMD:R_0805_HandSoldering (layer F.Cu)
-    (at 138.5 110 90)
+    (at 138.5 109 90)
     (descr "Resistor SMD 0805, hand soldering")
     (tags "resistor 0805")
     (attr smd)
-    (fp_text reference R10 (at 1.5 2 90) (layer F.SilkS)
+    (fp_text reference R10 (at 0 -2.5 180) (layer F.SilkS)
       (effects (font (size 1 1) (thickness 0.15)))
     )
@@
     (tags SOT-23)
     (attr smd)
-    (fp_text reference D2 (at 0 -2.5 180) (layer F.SilkS)
+    (fp_text reference D2 (at 2.6 -1.5 180) (layer F.SilkS)
       (effects (font (size 1 1) (thickness 0.15)))
     )
@@
     (tags SOT-23)
     (attr smd)
-    (fp_text reference D3 (at 0 -2.5) (layer F.SilkS)
+    (fp_text reference D3 (at 2 1.5 90) (layer F.SilkS)
       (effects (font (size 1 1) (thickness 0.15)))
     )
@@
   (gr_line (start 190 85) (end 190 135) (angle 90) (layer Edge.Cuts) (width 0.15))
   (gr_line (start 90 85) (end 190 85) (angle 90) (layer Edge.Cuts) (width 0.15))
+  (segment (start 145 120) (end 144 120) (width 0.25) (layer F.Cu) (net 1))
+  (via (at 144 120) (size 0.6) (drill 0.4) (layers F.Cu B.Cu) (net 1))
+  (segment (start 146 120) (end 145 120) (width 0.25) (layer B.Cu) (net 1))
+  (via (at 145 120) (size 0.6) (drill 0.4) (layers F.Cu B.Cu) (net 1))
+  (segment (start 147 120) (end 146 120) (width 0.25) (layer F.Cu) (net 1))
+  (via (at 146 120) (size 0.6) (drill 0.4) (layers F.Cu B.Cu) (net 1))
+  (segment (start 147 121) (end 147 120) (width 0.25) (layer B.Cu) (net 1))
+  (via (at 147 120) (size 0.6) (drill 0.4) (layers F.Cu B.Cu) (net 1))
+  (segment (start 147 122) (end 147 121) (width 0.25) (layer F.Cu) (net 1))
+  (via (at 147 121) (size 0.6) (drill 0.4) (layers F.Cu B.Cu) (net 1))
+  (segment (start 147 123) (end 147 122) (width 0.25) (layer B.Cu) (net 1))
+  (via (at 147 122) (size 0.6) (drill 0.4) (layers F.Cu B.Cu) (net 1))
+  (segment (start 149.25 124.5) (end 149.125 124.5) (width 0.25) (layer F.Cu) (net 1))
+  (segment (start 149.125 124.5) (end 147.625 123) (width 0.25) (layer F.Cu) (net 1))
+  (segment (start 147.625 123) (end 147 123) (width 0.25) (layer F.Cu) (net 1))
+  (via (at 147 123) (size 0.6) (drill 0.4) (layers F.Cu B.Cu) (net 1))
+  (segment (start 149.25 124.5) (end 148 124.5) (width 0.25) (layer F.Cu) (net 1))
   (segment (start 103.5 134) (end 104.5 134) (width 0.25) (layer F.Cu) (net 1))
   (segment (start 91.5 109) (end 91.5 108.5) (width 0.25) (layer F.Cu) (net 1))
@@
   (segment (start 163.85 120.5) (end 163.85 118.2) (width 0.6) (layer F.Cu) (net 9))
   (segment (start 163.85 118.2) (end 163.6 117.95) (width 0.6) (layer F.Cu) (net 9))
+  (segment (start 138.5 111.35) (end 138.5 110.35) (width 1) (layer F.Cu) (net 10))
   (segment (start 140 113.05) (end 137.95 113.05) (width 1) (layer F.Cu) (net 10))
   (segment (start 137.95 113.05) (end 137.5 113.5) (width 1) (layer F.Cu) (net 10))
@@
     )
     (polygon
-      (pts        (xy 139 110) (xy 139 117) (xy 148.5 117.5) (xy 148.5 121.5) (xy 150.5 121.5)
+      (pts        (xy 139 110) (xy 139 117) (xy 148.5 117) (xy 148.5 121.5) (xy 150.5 121.5)
         (xy 150.5 125) (xy 155 125) (xy 155 119) (xy 154.5 117) (xy 154.5 113)
         (xy 140 113) (xy 140 110)
